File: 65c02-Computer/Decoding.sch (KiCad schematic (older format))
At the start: 1 part, among them U3 74LS04

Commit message: Connected VIA
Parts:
- added U?: 74LS32, symbol 74xx:74LS32
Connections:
- net A15: now also U?.1
- new net A13: U?.2
- new net V1_CS2B: U?.3
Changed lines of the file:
@@
 EESchema Schematic File Version 4
+LIBS:65c02-Computer-cache
 EELAYER 30 0
 EELAYER END
@@
 Wire Wire Line
 	4600 3700 5200 3700
+Text HLabel 4600 3950 0    50   Input ~ 0
+A14
+Text HLabel 5200 3950 2    50   Output ~ 0
+V1_CS1
+Wire Wire Line
+	4600 3950 5200 3950
+$Comp
+L 74xx:74LS32 U?
+U 1 1 5DD09F52
+P 4900 4350
+F 0 "U?" H 4900 4675 50  0000 C CNN
+F 1 "74LS32" H 4900 4584 50  0000 C CNN
+F 2 "" H 4900 4350 50  0001 C CNN
+F 3 "http://www.ti.com/lit/gpn/sn74LS32" H 4900 4350 50  0001 C CNN
+	1    4900 4350
+	1    0    0    -1
+$EndComp
+Text HLabel 4600 4250 0    50   Input ~ 0
+A15
+Text HLabel 4600 4450 0    50   Input ~ 0
+A13
+Text HLabel 5200 4350 2    50   Output ~ 0
+V1_CS2B
 $EndSCHEMATC

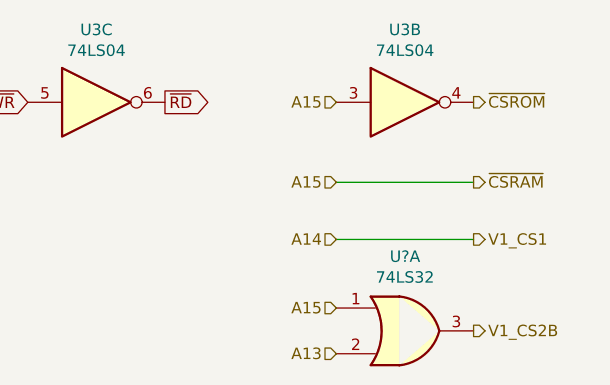
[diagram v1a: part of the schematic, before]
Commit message: Rename clock signals and add annotations
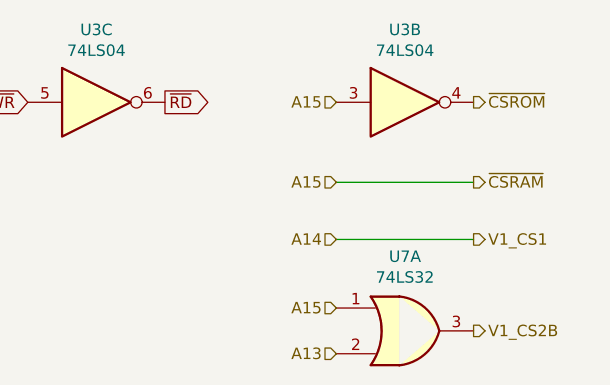
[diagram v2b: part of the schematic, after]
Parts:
- gave numbers to parts that had none: 1
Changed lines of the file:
@@
 	4600 3950 5200 3950
 $Comp
-L 74xx:74LS32 U?
+L 74xx:74LS32 U7
 U 1 1 5DD09F52
 P 4900 4350
-F 0 "U?" H 4900 4675 50  0000 C CNN
+F 0 "U7" H 4900 4675 50  0000 C CNN
 F 1 "74LS32" H 4900 4584 50  0000 C CNN
 F 2 "" H 4900 4350 50  0001 C CNN

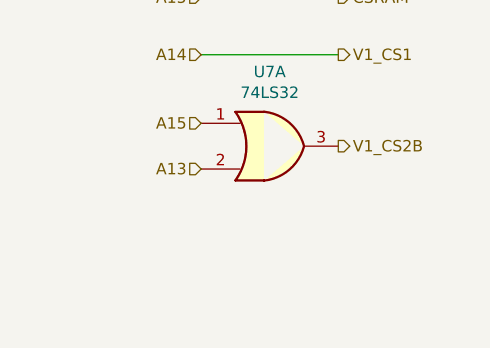
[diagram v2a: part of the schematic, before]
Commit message: Update pcb and put arduino sketch
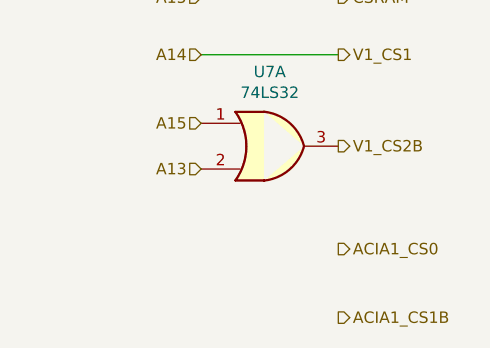
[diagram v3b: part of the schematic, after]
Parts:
- U7: footprint (none) -> Package_DIP:DIP-14_W7.62mm_LongPads
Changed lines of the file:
@@
 F 0 "U7" H 4900 4675 50  0000 C CNN
 F 1 "74LS32" H 4900 4584 50  0000 C CNN
-F 2 "" H 4900 4350 50  0001 C CNN
+F 2 "Package_DIP:DIP-14_W7.62mm_LongPads" H 4900 4350 50  0001 C CNN
 F 3 "http://www.ti.com/lit/gpn/sn74LS32" H 4900 4350 50  0001 C CNN
 	1    4900 4350
@@
 Text HLabel 5200 4350 2    50   Output ~ 0
 V1_CS2B
+Text HLabel 5200 4800 2    50   Output ~ 0
+ACIA1_CS0
+Text HLabel 5200 5100 2    50   Output ~ 0
+ACIA1_CS1B
 $EndSCHEMATC

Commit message: Create v2
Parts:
- removed U7: 74LS32, Package_DIP:DIP-14_W7.62mm_LongPads, symbol 74xx:74LS32
- added U10: 74LS138, Package_DIP:DIP-16_W7.62mm_LongPads, symbol 74xx:74LS138
- added U9: 74LS30, Package_DIP:DIP-14_W7.62mm_LongPads, symbol 74xx:74LS30
- renumbered U3 to U8
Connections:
- net A13: now also U9.2
- net A14: now also U9.1
- net ACIA1_CS1B: now also U10.10 (O5)
- net V1_CS2B: now also U10.7 (O7)
- net ~CSROM: now also U9.12
- new net: U10.5 (E2), U9.8
- new net +5V: U10.16 (VCC), U10.6 (E3)
- new net A10: U9.5
- new net A11: U9.4
- new net A12: U9.3
- new net A5: U10.1 (A0)
- new net A6: U10.2 (A1)
- new net A7: U10.3 (A2)
- new net A8: U9.11
- new net A9: U9.6
- new net GND: U10.4 (E1), U10.8 (GND)
- new net V2_CS2B: U10.9 (O6)
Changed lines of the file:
@@
 P 4900 3350
 AR Path="/5DCDA2AA" Ref="U?"  Part="2"
-AR Path="/5DCD4933/5DCDA2AA" Ref="U3"  Part="2"
-F 0 "U3" H 4900 3667 50  0000 C CNN
+AR Path="/5DCD4933/5DCDA2AA" Ref="U8"  Part="2"
+F 0 "U8" H 4900 3667 50  0000 C CNN
 F 1 "74LS04" H 4900 3576 50  0000 C CNN
 F 2 "Package_DIP:DIP-14_W7.62mm" H 4900 3350 50  0001 C CNN
@@
 P 3550 3350
 AR Path="/5DCDA2B0" Ref="U?"  Part="3"
-AR Path="/5DCD4933/5DCDA2B0" Ref="U3"  Part="3"
-F 0 "U3" H 3550 3667 50  0000 C CNN
+AR Path="/5DCD4933/5DCDA2B0" Ref="U8"  Part="3"
+F 0 "U8" H 3550 3667 50  0000 C CNN
 F 1 "74LS04" H 3550 3576 50  0000 C CNN
 F 2 "Package_DIP:DIP-14_W7.62mm" H 3550 3350 50  0001 C CNN
@@
 Wire Wire Line
 	4600 3700 5200 3700
-Text HLabel 4600 3950 0    50   Input ~ 0
+Text HLabel 4700 5400 2    50   Output ~ 0
+V1_CS2B
+Text HLabel 4700 5200 2    50   Output ~ 0
+ACIA1_CS1B
+Text HLabel 4700 5300 2    50   Output ~ 0
+V2_CS2B
+Text HLabel 2800 5000 0    50   Input ~ 0
 A14
-Text HLabel 5200 3950 2    50   Output ~ 0
-V1_CS1
+Text HLabel 2800 5100 0    50   Input ~ 0
+A13
+Text HLabel 2800 5200 0    50   Input ~ 0
+A12
+Text HLabel 2800 5300 0    50   Input ~ 0
+A11
+Text HLabel 2800 5400 0    50   Input ~ 0
+A10
+Text HLabel 2800 5500 0    50   Input ~ 0
+A9
+Text HLabel 2800 5600 0    50   Input ~ 0
+A8
 Wire Wire Line
-	4600 3950 5200 3950
+	3400 5300 3700 5300
+Wire Wire Line
+	3700 5200 3600 5200
+Wire Wire Line
+	3700 5400 3600 5400
 $Comp
-L 74xx:74LS32 U7
-U 1 1 5DD09F52
-P 4900 4350
-F 0 "U7" H 4900 4675 50  0000 C CNN
-F 1 "74LS32" H 4900 4584 50  0000 C CNN
-F 2 "Package_DIP:DIP-14_W7.62mm_LongPads" H 4900 4350 50  0001 C CNN
-F 3 "http://www.ti.com/lit/gpn/sn74LS32" H 4900 4350 50  0001 C CNN
-	1    4900 4350
+L power:GND #PWR043
+U 1 1 5DD27F13
+P 4200 5700
+F 0 "#PWR043" H 4200 5450 50  0001 C CNN
+F 1 "GND" H 4205 5527 50  0000 C CNN
+F 2 "" H 4200 5700 50  0001 C CNN
+F 3 "" H 4200 5700 50  0001 C CNN
+	1    4200 5700
 	1    0    0    -1
 $EndComp
-Text HLabel 4600 4250 0    50   Input ~ 0
-A15
-Text HLabel 4600 4450 0    50   Input ~ 0
-A13
-Text HLabel 5200 4350 2    50   Output ~ 0
-V1_CS2B
-Text HLabel 5200 4800 2    50   Output ~ 0
-ACIA1_CS0
-Text HLabel 5200 5100 2    50   Output ~ 0
-ACIA1_CS1B
+$Comp
+L power:+5V #PWR042
+U 1 1 5DD28639
+P 4200 4400
+F 0 "#PWR042" H 4200 4250 50  0001 C CNN
+F 1 "+5V" H 4215 4573 50  0000 C CNN
+F 2 "" H 4200 4400 50  0001 C CNN
+F 3 "" H 4200 4400 50  0001 C CNN
+	1    4200 4400
+	1    0    0    -1
+$EndComp
+Text HLabel 2800 5700 0    50   Input ~ 0
+~CSROM
+$Comp
+L 74xx:74LS30 U9
+U 1 1 5DD0D689
+P 3100 5300
+F 0 "U9" H 3100 5825 50  0000 C CNN
+F 1 "74LS30" H 3100 5734 50  0000 C CNN
+F 2 "Package_DIP:DIP-14_W7.62mm_LongPads" H 3100 5300 50  0001 C CNN
+F 3 "http://www.ti.com/lit/gpn/sn74LS30" H 3100 5300 50  0001 C CNN
+	1    3100 5300
+	1    0    0    -1
+$EndComp
+Text HLabel 3700 4900 0    50   Input ~ 0
+A7
+Text HLabel 3700 4700 0    50   Input ~ 0
+A5
+Text HLabel 3700 4800 0    50   Input ~ 0
+A6
+$Comp
+L 74xx:74LS138 U10
+U 1 1 5DD2E6BB
+P 4200 5000
+F 0 "U10" H 4200 5781 50  0000 C CNN
+F 1 "74LS138" H 4200 5690 50  0000 C CNN
+F 2 "Package_DIP:DIP-16_W7.62mm_LongPads" H 4200 5000 50  0001 C CNN
+F 3 "http://www.ti.com/lit/gpn/sn74LS138" H 4200 5000 50  0001 C CNN
+	1    4200 5000
+	1    0    0    -1
+$EndComp
+$Comp
+L power:+5V #PWR040
+U 1 1 5DD2F229
+P 3600 5200
+F 0 "#PWR040" H 3600 5050 50  0001 C CNN
+F 1 "+5V" H 3615 5373 50  0000 C CNN
+F 2 "" H 3600 5200 50  0001 C CNN
+F 3 "" H 3600 5200 50  0001 C CNN
+	1    3600 5200
+	1    0    0    -1
+$EndComp
+$Comp
+L power:GND #PWR041
+U 1 1 5DD2F5CF
+P 3600 5400
+F 0 "#PWR041" H 3600 5150 50  0001 C CNN
+F 1 "GND" H 3605 5227 50  0000 C CNN
+F 2 "" H 3600 5400 50  0001 C CNN
+F 3 "" H 3600 5400 50  0001 C CNN
+	1    3600 5400
+	1    0    0    -1
+$EndComp
 $EndSCHEMATC
